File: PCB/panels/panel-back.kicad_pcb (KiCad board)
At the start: 2 copper layers, 140 x 35 mm, 6 parts

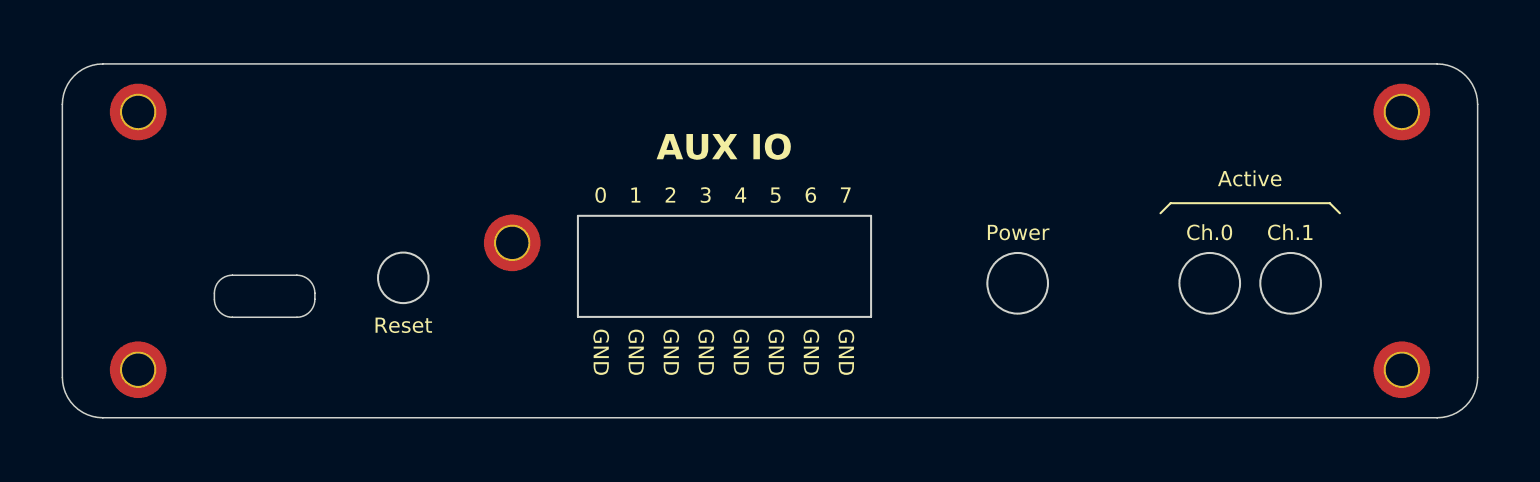
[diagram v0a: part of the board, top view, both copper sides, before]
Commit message: Rev C First Draft
- Fix and move LED footprints
- Move bar code sticker
- Add op-amp unity voltage follower to ADC input
- Remove screw terminals
- Made panel screw holes bigger both panels (3.2mm -> 3.7mm) for 3.4mm
  screws
- Create cutout for mounting rail on panels
- Delete the file with both back and front panels
- Update all footprints (except rp2354b so that its thermal vias pass DRC)
- Add component class and custom rule for USB-C footprint
- Indicate M3 screw in schematic + Add to BOM
- Improve adherence to ADC/DAC datasheets:
  - Move high speed signals out from under ADC (put MISO in +5V layer under ADC)
  - Add 10uF decoupling caps to ADC/DAC
- Change enclosure part number to black enclosure
- Add some more GND vias to isolated GND planes
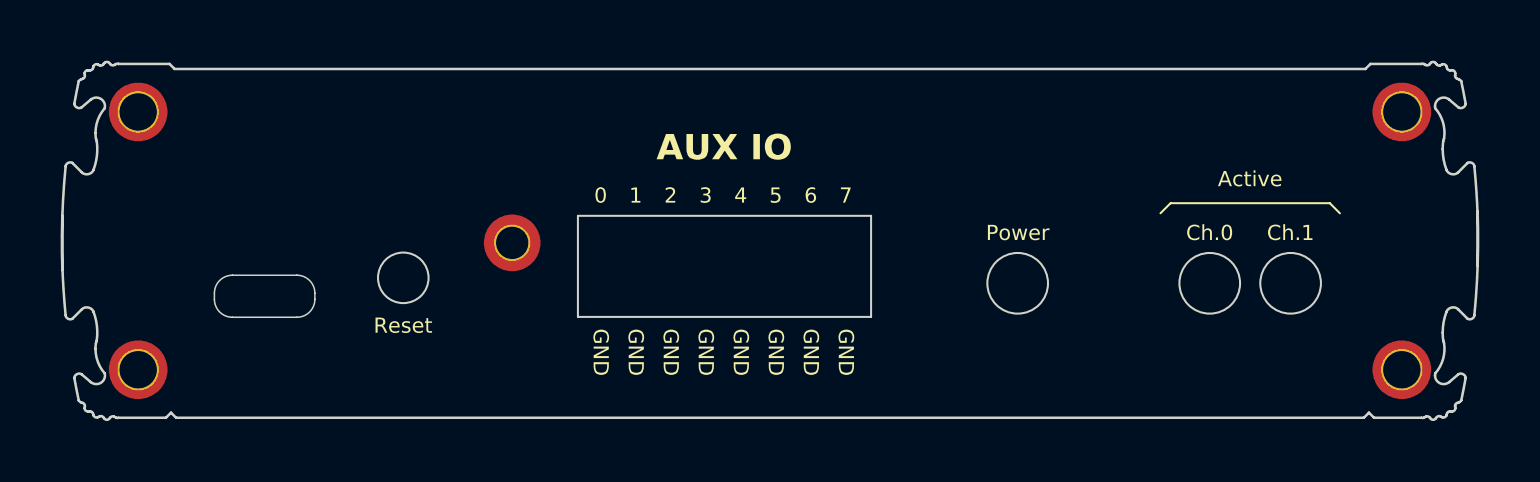
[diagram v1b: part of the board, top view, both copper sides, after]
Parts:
- REF** (x4): value MountingHole_3.2mm_M3_DIN965_Pad_TopOnly -> MountingHole_3.7mm_Pad_TopOnly_EXN-23359; footprint MountingHole:MountingHole_3.2mm_M3_DIN965_Pad_TopOnly -> open-ephys:MountingHole_3.7mm_Pad_TopOnly_EXN-23359
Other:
- board size 140 x 35 mm -> 140.1 x 35.4 mm

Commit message: fix panel outline
Remove the finer features that might not
adhere to best practices for PCB DFM
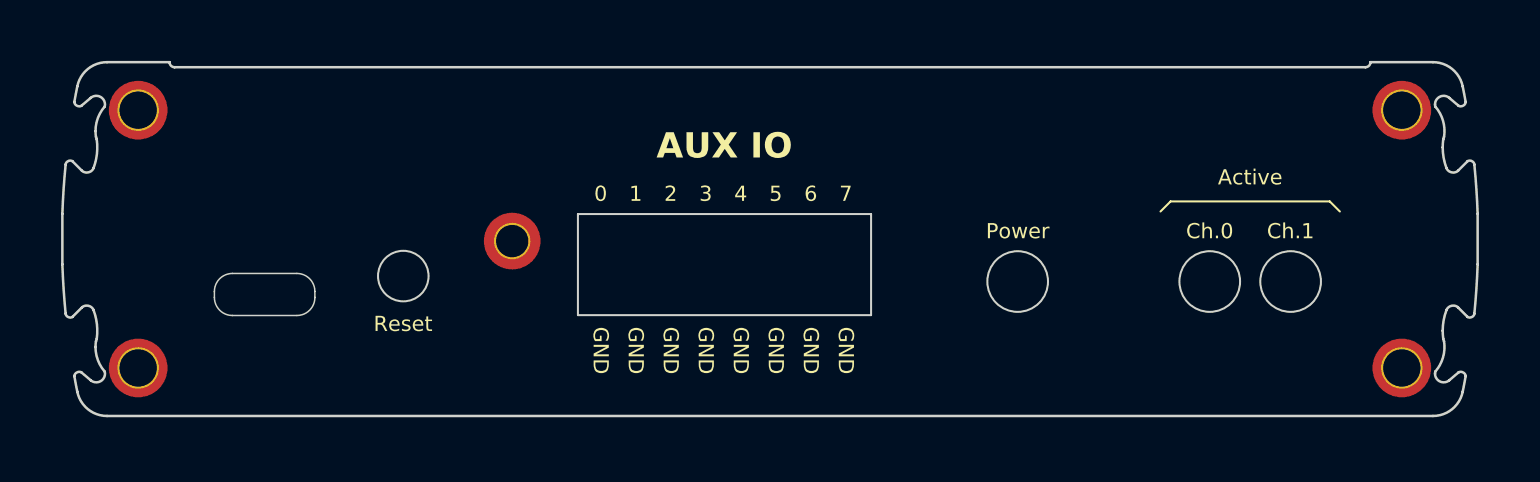
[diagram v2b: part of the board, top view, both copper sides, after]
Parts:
- moved G*** 0.18 mm to (102.8, 51.4)
- moved REF** 0.17 mm to (86.5, 72.8)
- moved REF** 0.17 mm to (211.5, 72.8)
- moved REF** 0.17 mm to (211.5, 47.2)
- moved REF** 0.17 mm to (123.5, 60.2)
- moved REF** 0.17 mm to (86.5, 47.2)
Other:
- board size 140.1 x 35.4 mm -> 140 x 35 mm
